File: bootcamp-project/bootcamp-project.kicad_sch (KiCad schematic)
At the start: 1 part

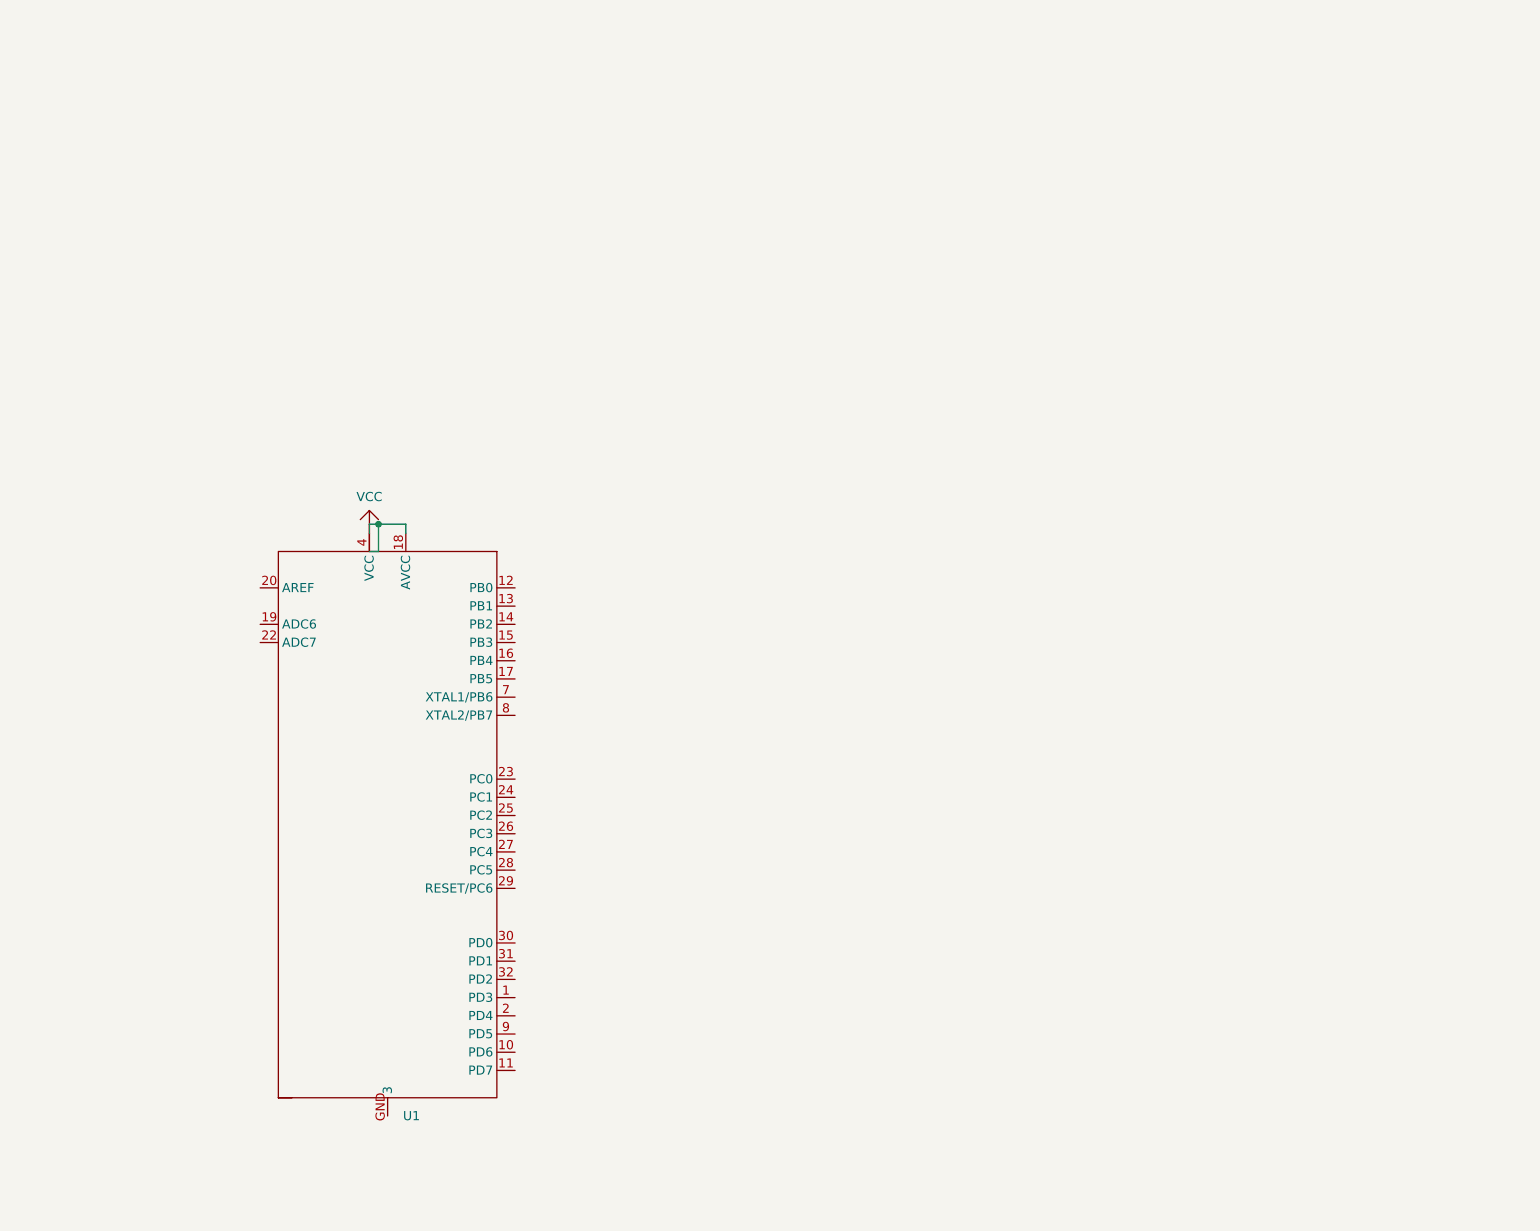
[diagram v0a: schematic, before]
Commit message: schematic: input/output not driven
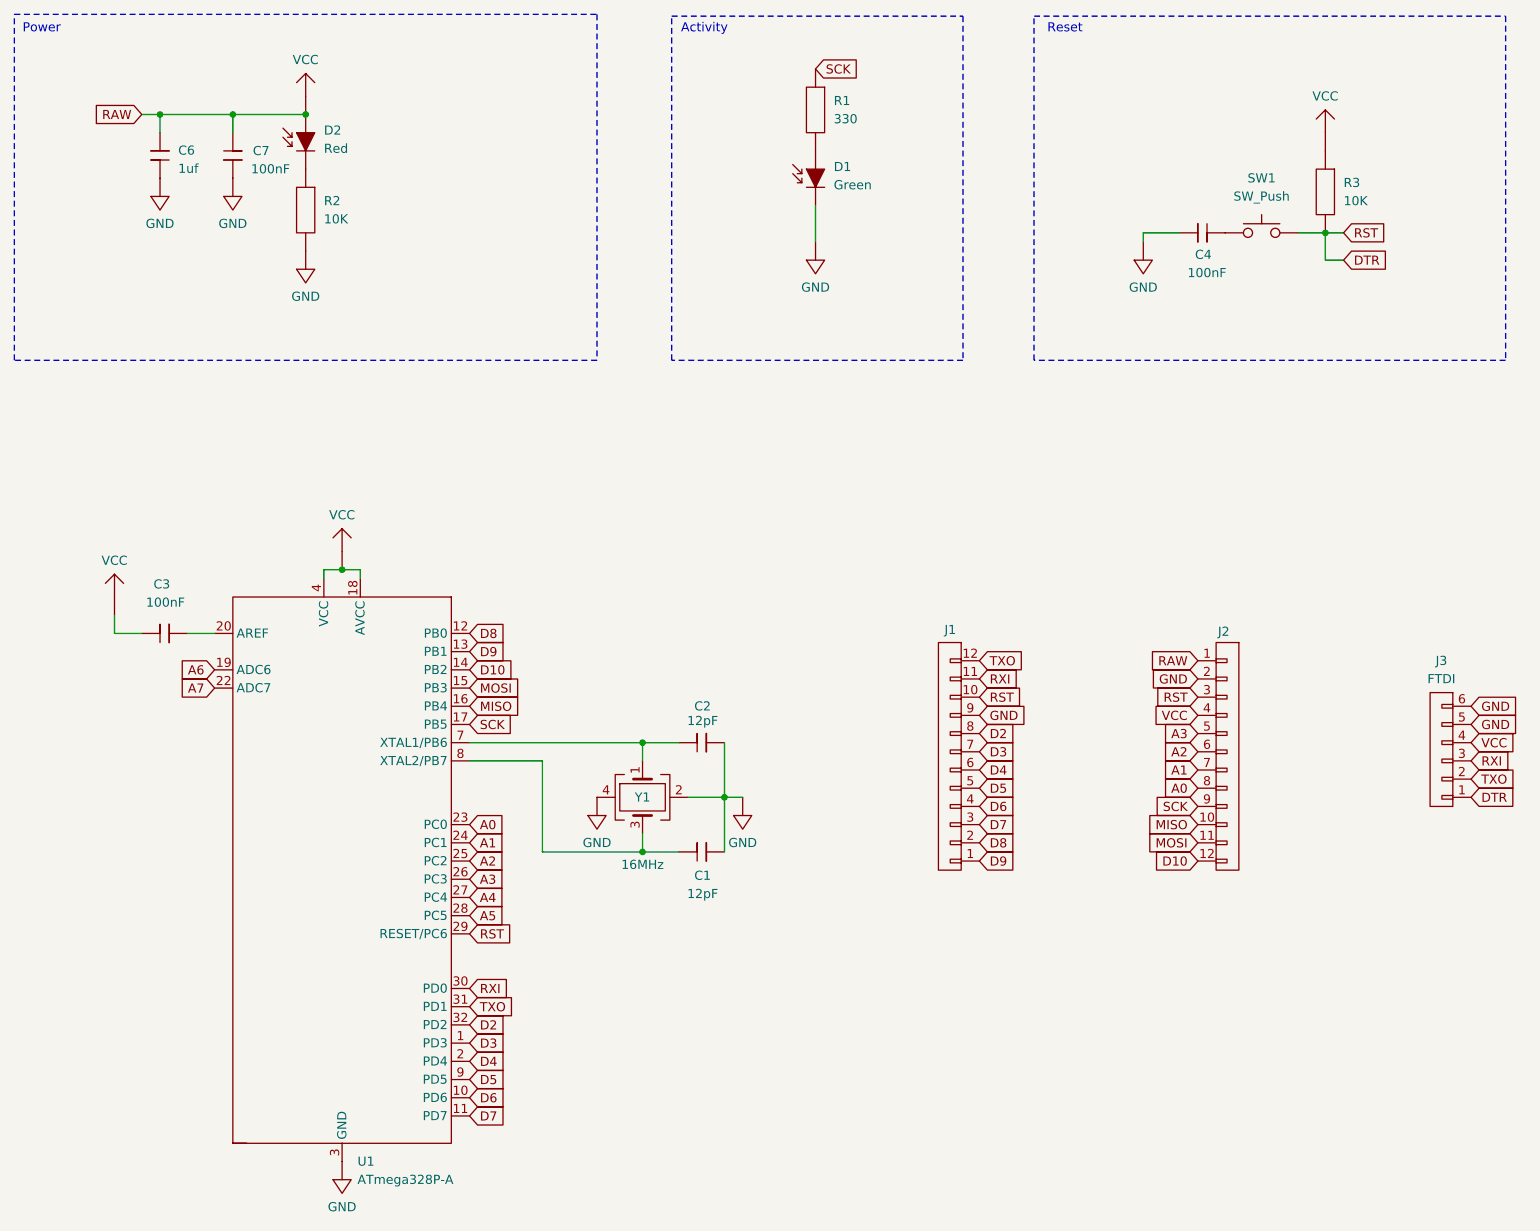
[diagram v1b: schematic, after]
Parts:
- added C1, C2: 12pF, symbol bootcamp00:CAPACITOR
- added C3, C4, C7: 100nF, symbol bootcamp00:CAPACITOR
- added C6: 1uf, symbol bootcamp00:CAPACITOR
- added D1: Green, symbol bootcamp00:DIODE_LIGHT_EMITTING
- added D2: Red, symbol bootcamp00:DIODE_LIGHT_EMITTING
- added J1: ~, symbol bootcamp00:JUMPER1
- added J2: ~, symbol bootcamp00:JUMPER2
- added J3: FTDI, symbol bootcamp00:JUMPER3
- added R1: 330, symbol bootcamp00:RESISTOR
- added R2, R3: 10K, symbol bootcamp00:RESISTOR
- added SW1: SW_Push, symbol bootcamp00:SWITCH
- added Y1: 16MHz, symbol bootcamp00:QUARTZ
- U1: value ~ -> ATmega328P-A
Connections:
- net D3: now reaches U1.1 (PD3)
- net D3: now also J1.7
- net D6: now reaches U1.10 (PD6)
- net D6: now also J1.4
- net D7: now reaches U1.11 (PD7)
- net D7: now also J1.3
- net D8: now reaches U1.12 (PB0)
- net D8: now also J1.2
- net D9: now reaches U1.13 (PB1)
- net D9: now also J1.1
- net D10: now reaches U1.14 (PB2)
- net D10: now also J2.12
- net MOSI: now reaches U1.15 (PB3)
- net MOSI: now also J2.11
- net MISO: now reaches U1.16 (PB4)
- net MISO: now also J2.10
- net SCK: now reaches U1.17 (PB5)
- net SCK: now also J2.9, R1.0
- net A6: now reaches U1.19 (ADC6)
- net D4: now reaches U1.2 (PD4)
- net D4: now also J1.6
- net at U1.20 (AREF): now also C3.1
- net A7: now reaches U1.22 (ADC7)
- net A0: now reaches U1.23 (PC0)
- net A0: now also J2.8
- net A1: now reaches U1.24 (PC1)
- net A1: now also J2.7
- net A2: now reaches U1.25 (PC2)
- net A2: now also J2.6
- net A3: now reaches U1.26 (PC3)
- net A3: now also J2.5
- net A4: now reaches U1.27 (PC4)
- net A5: now reaches U1.28 (PC5)
- net DTR: now reaches U1.29 (RESET/PC6)
- net DTR: now also J1.10, J2.3, J3.1, R3.1, SW1.1
- net RXI: now reaches U1.30 (PD0)
- net RXI: now also J1.11, J3.3
- net TXO: now reaches U1.31 (PD1)
- net TXO: now also J1.12, J3.2
- net D2: now reaches U1.32 (PD2)
- net D2: now also J1.8
- net at U1.7 (XTAL1/PB6): now also C2.0, Y1.1
- net at U1.8 (XTAL2/PB7): now also C1.0, Y1.3
- net D5: now reaches U1.9 (PD5)
- net D5: now also J1.5
- new net: D1.0, R1.1
- new net: C1.1, C2.1, Y1.2
- new net: C4.0, SW1.0
- new net: D2.1, R2.0
- new net GND: J1.9, J2.2, J3.5, J3.6
- new net RAW: C6.1, C7.0, D2.0, J2.1
- new net VCC: J2.4, J3.4
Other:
- note added: "Activity"
- note added: "Power"
- note added: "Reset"

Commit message: all: general fix, no more EDR errors
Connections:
- net RAW: now also C6.0; no longer C6.1
- net at C4.0: no longer SW1.0
- net at C4.1: now also SW1.0
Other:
- moved on the sheet: C4, C6
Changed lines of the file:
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@@
 	(symbol
 		(lib_id "bootcamp00:CAPACITOR")
-		(at 186.69 53.34 270)
+		(at 185.42 48.26 90)
 		(unit 1)
 		(exclude_from_sim no)
@@
 		(dnp no)
 		(property "Reference" "C4"
-			(at 186.182 53.848 90)
+			(at 185.928 47.752 90)
 			(effects
 				(font
@@
 		)
 		(property "Value" "100nF"
-			(at 186.69 56.388 90)
+			(at 185.42 45.212 90)
 			(effects
 				(font
@@
 		)
 		(property "Footprint" ""
-			(at 186.69 53.34 0)
+			(at 185.42 48.26 0)
 			(effects
 				(font
@@
 		)
 		(property "Datasheet" ""
-			(at 186.69 53.34 0)
+			(at 185.42 48.26 0)
 			(effects
 				(font
@@
 		)
 		(property "Description" ""
-			(at 186.69 53.34 0)
+			(at 185.42 48.26 0)
 			(effects
 				(font
@@
 	(symbol
 		(lib_id "bootcamp00:CAPACITOR")
-		(at 38.1 40.64 180)
+		(at 43.18 39.37 0)
 		(unit 1)
 		(exclude_from_sim no)
@@
 		(on_board yes)
 		(dnp no)
-		(fields_autoplaced yes)
 		(property "Reference" "C6"
-			(at 43.18 39.3064 0)
+			(at 43.18 39.37 0)
 			(effects
 				(font
 					(size 1.27 1.27)
 				)
-				(justify right)
+				(justify left)
 			)
 		)
 		(property "Value" "1uf"
-			(at 43.18 41.8464 0)
+			(at 43.18 41.656 0)
 			(effects
 				(font
 					(size 1.27 1.27)
 				)
-				(justify right)
+				(justify left)
 			)
 		)
 		(property "Footprint" ""
-			(at 38.1 40.64 0)
+			(at 43.18 39.37 0)
 			(effects
 				(font
@@
 		)
 		(property "Datasheet" ""
-			(at 38.1 40.64 0)
+			(at 43.18 39.37 0)
 			(effects
 				(font
@@
 		)
 		(property "Description" ""
-			(at 38.1 40.64 0)
+			(at 43.18 39.37 0)
 			(effects
 				(font
